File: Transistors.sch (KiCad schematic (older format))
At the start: 5 parts, among them T1 L298, T2 L298, T3 L298, T4 L298, T5 L298

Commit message: New schematics: Top and Controller
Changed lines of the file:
@@
 EESchema Schematic File Version 2
-LIBS:L298
 LIBS:power
 LIBS:device
@@
 LIBS:contrib
 LIBS:valves
-LIBS:Stepper Motor Driver-cache
+LIBS:L298
 EELAYER 25 0
 EELAYER END
 $Descr A4 11693 8268
 encoding utf-8
-Sheet 1 2
+Sheet 1 1
 Title ""
 Date ""
@@
 	1    0    0    -1
 $EndComp
-Text GLabel 1600 1500 0    60   Input ~ 0
+Text HLabel 1600 1600 0    60   Input ~ 0
+T1_Enable_A
+Text HLabel 1600 1700 0    60   Input ~ 0
+T1_Input_2
+Text HLabel 1600 1900 0    60   Input ~ 0
+T1_Input_3
+Text HLabel 1600 2000 0    60   Input ~ 0
+T1_Enable_B
+Text HLabel 1600 2100 0    60   Input ~ 0
+T1_Input_4
+Text HLabel 3650 1500 2    60   Input ~ 0
+T1_Output_1
+Text HLabel 3650 1600 2    60   Input ~ 0
+T1_Output_2
+Text HLabel 3650 1900 2    60   Input ~ 0
+T1_Output_3
+Text HLabel 3650 2000 2    60   Input ~ 0
+T1_Output_4
+Wire Wire Line
+	1600 1500 1900 1500
+Wire Wire Line
+	1600 1600 1900 1600
+Wire Wire Line
+	1600 1700 1900 1700
+Wire Wire Line
+	1600 1900 1900 1900
+Wire Wire Line
+	1600 2000 1900 2000
+Wire Wire Line
+	1600 2100 1900 2100
+Wire Wire Line
+	3400 1500 3650 1500
+Wire Wire Line
+	3400 1600 3650 1600
+Wire Wire Line
+	3400 1900 3650 1900
+Wire Wire Line
+	3400 2000 3650 2000
+Text HLabel 1600 3600 0    60   Input ~ 0
+T2_Input_1
+Text HLabel 1600 3700 0    60   Input ~ 0
+T2_Enable_A
+Text HLabel 1600 3800 0    60   Input ~ 0
+T2_Input_2
+Text HLabel 1600 4000 0    60   Input ~ 0
+T2_Input_3
+Text HLabel 1600 4100 0    60   Input ~ 0
+T2_Enable_B
+Text HLabel 1600 4200 0    60   Input ~ 0
+T2_Input_4
+Wire Wire Line
+	1600 3600 1900 3600
+Wire Wire Line
+	1600 3700 1900 3700
+Wire Wire Line
+	1600 3800 1900 3800
+Wire Wire Line
+	1600 4000 1900 4000
+Wire Wire Line
+	1600 4100 1900 4100
+Wire Wire Line
+	1600 4200 1900 4200
+Text HLabel 1600 5700 0    60   Input ~ 0
+T3_Input_1
+Text HLabel 1600 5800 0    60   Input ~ 0
+T3_Enable_A
+Text HLabel 1600 5900 0    60   Input ~ 0
+T3_Input_2
+Text HLabel 1600 6100 0    60   Input ~ 0
+T3_Input_3
+Text HLabel 1600 6200 0    60   Input ~ 0
+T3_Enable_B
+Text HLabel 1600 6300 0    60   Input ~ 0
+T3_Input_4
+Wire Wire Line
+	1600 5700 1900 5700
+Wire Wire Line
+	1600 5800 1900 5800
+Wire Wire Line
+	1600 5900 1900 5900
+Wire Wire Line
+	1600 6100 1900 6100
+Wire Wire Line
+	1600 6200 1900 6200
+Wire Wire Line
+	1600 6300 1900 6300
+Text HLabel 3650 3600 2    60   Input ~ 0
+T2_Output_1
+Text HLabel 3650 3700 2    60   Input ~ 0
+T2_Output_2
+Text HLabel 3650 4000 2    60   Input ~ 0
+T2_Output_3
+Text HLabel 3650 4100 2    60   Input ~ 0
+T2_Output_4
+Wire Wire Line
+	3400 3600 3650 3600
+Wire Wire Line
+	3400 3700 3650 3700
+Wire Wire Line
+	3400 4000 3650 4000
+Wire Wire Line
+	3400 4100 3650 4100
+Text HLabel 3650 5700 2    60   Input ~ 0
+T3_Output_1
+Text HLabel 3650 5800 2    60   Input ~ 0
+T3_Output_2
+Text HLabel 3650 6100 2    60   Input ~ 0
+T3_Output_3
+Text HLabel 3650 6200 2    60   Input ~ 0
+T3_Output_4
+Wire Wire Line
+	3400 5700 3650 5700
+Wire Wire Line
+	3400 5800 3650 5800
+Wire Wire Line
+	3400 6100 3650 6100
+Wire Wire Line
+	3400 6200 3650 6200
+Text HLabel 8100 1600 2    60   Input ~ 0
+T4_Output_1
+Text HLabel 8100 1700 2    60   Input ~ 0
+T4_Output_2
+Text HLabel 8100 2000 2    60   Input ~ 0
+T4_Output_3
+Text HLabel 8100 2100 2    60   Input ~ 0
+T4_Output_4
+Wire Wire Line
+	7850 1600 8100 1600
+Wire Wire Line
+	7850 1700 8100 1700
+Wire Wire Line
+	7850 2000 8100 2000
+Wire Wire Line
+	7850 2100 8100 2100
+Text HLabel 8100 3650 2    60   Input ~ 0
+T5_Output_1
+Text HLabel 8100 3750 2    60   Input ~ 0
+T5_Output_2
+Text HLabel 8100 4050 2    60   Input ~ 0
+T5_Output_3
+Text HLabel 8100 4150 2    60   Input ~ 0
+T5_Output_4
+Wire Wire Line
+	7850 3650 8100 3650
+Wire Wire Line
+	7850 3750 8100 3750
+Wire Wire Line
+	7850 4050 8100 4050
+Wire Wire Line
+	7850 4150 8100 4150
+Text HLabel 6050 1600 0    60   Input ~ 0
+T4_Input_1
+Text HLabel 6050 1700 0    60   Input ~ 0
+T4_Enable_A
+Text HLabel 6050 1800 0    60   Input ~ 0
+T4_Input_2
+Text HLabel 6050 2000 0    60   Input ~ 0
+T4_Input_3
+Text HLabel 6050 2100 0    60   Input ~ 0
+T4_Enable_B
+Text HLabel 6050 2200 0    60   Input ~ 0
+T4_Input_4
+Wire Wire Line
+	6050 1600 6350 1600
+Wire Wire Line
+	6050 1700 6350 1700
+Wire Wire Line
+	6050 1800 6350 1800
+Wire Wire Line
+	6050 2000 6350 2000
+Wire Wire Line
+	6050 2100 6350 2100
+Wire Wire Line
+	6050 2200 6350 2200
+Text HLabel 6050 3650 0    60   Input ~ 0
+T5_Input_1
+Text HLabel 6050 3750 0    60   Input ~ 0
+T5_Enable_A
+Text HLabel 6050 3850 0    60   Input ~ 0
+T5_Input_2
+Text HLabel 6050 4050 0    60   Input ~ 0
+T5_Input_3
+Text HLabel 6050 4150 0    60   Input ~ 0
+T5_Enable_B
+Text HLabel 6050 4250 0    60   Input ~ 0
+T5_Input_4
+Wire Wire Line
+	6050 3650 6350 3650
+Wire Wire Line
+	6050 3750 6350 3750
+Wire Wire Line
+	6050 3850 6350 3850
+Wire Wire Line
+	6050 4050 6350 4050
+Wire Wire Line
+	6050 4150 6350 4150
+Wire Wire Line
+	6050 4250 6350 4250
+Text HLabel 1600 1500 0    60   Input ~ 0
 T1_Input_1
-Text GLabel 1600 1600 0    60   Input ~ 0
-T1_Enable_A
-Text GLabel 1600 1700 0    60   Input ~ 0
-T1_Input_2
-Text GLabel 1600 1900 0    60   Input ~ 0
-T1_Input_3
-Text GLabel 1600 2000 0    60   Input ~ 0
-T1_Enable_B
-Text GLabel 1600 2100 0    60   Input ~ 0
-T1_Input_4
-Text GLabel 3650 1500 2    60   Input ~ 0
-T1_Output_1
-Text GLabel 3650 1600 2    60   Input ~ 0
-T1_Output_2
-Text GLabel 3650 1900 2    60   Input ~ 0
-T1_Output_3
-Text GLabel 3650 2000 2    60   Input ~ 0
-T1_Output_4
-Wire Wire Line
-	1600 1500 1900 1500
-Wire Wire Line
-	1600 1600 1900 1600
-Wire Wire Line
-	1600 1700 1900 1700
-Wire Wire Line
-	1600 1900 1900 1900
-Wire Wire Line
-	1600 2000 1900 2000
-Wire Wire Line
-	1600 2100 1900 2100
-Wire Wire Line
-	3400 1500 3650 1500
-Wire Wire Line
-	3400 1600 3650 1600
-Wire Wire Line
-	3400 1900 3650 1900
-Wire Wire Line
-	3400 2000 3650 2000
-Text GLabel 1600 3600 0    60   Input ~ 0
-T2_Input_1
-Text GLabel 1600 3700 0    60   Input ~ 0
-T2_Enable_A
-Text GLabel 1600 3800 0    60   Input ~ 0
-T2_Input_2
-Text GLabel 1600 4000 0    60   Input ~ 0
-T2_Input_3
-Text GLabel 1600 4100 0    60   Input ~ 0
-T2_Enable_B
-Text GLabel 1600 4200 0    60   Input ~ 0
-T2_Input_4
-Wire Wire Line
-	1600 3600 1900 3600
-Wire Wire Line
-	1600 3700 1900 3700
-Wire Wire Line
-	1600 3800 1900 3800
-Wire Wire Line
-	1600 4000 1900 4000
-Wire Wire Line
-	1600 4100 1900 4100
-Wire Wire Line
-	1600 4200 1900 4200
-Text GLabel 1600 5700 0    60   Input ~ 0
-T3_Input_1
-Text GLabel 1600 5800 0    60   Input ~ 0
-T3_Enable_A
-Text GLabel 1600 5900 0    60   Input ~ 0
-T3_Input_2
-Text GLabel 1600 6100 0    60   Input ~ 0
-T3_Input_3
-Text GLabel 1600 6200 0    60   Input ~ 0
-T3_Enable_B
-Text GLabel 1600 6300 0    60   Input ~ 0
-T3_Input_4
-Wire Wire Line
-	1600 5700 1900 5700
-Wire Wire Line
-	1600 5800 1900 5800
-Wire Wire Line
-	1600 5900 1900 5900
-Wire Wire Line
-	1600 6100 1900 6100
-Wire Wire Line
-	1600 6200 1900 6200
-Wire Wire Line
-	1600 6300 1900 6300
-Text GLabel 3650 3600 2    60   Input ~ 0
-T2_Output_1
-Text GLabel 3650 3700 2    60   Input ~ 0
-T2_Output_2
-Text GLabel 3650 4000 2    60   Input ~ 0
-T2_Output_3
-Text GLabel 3650 4100 2    60   Input ~ 0
-T2_Output_4
-Wire Wire Line
-	3400 3600 3650 3600
-Wire Wire Line
-	3400 3700 3650 3700
-Wire Wire Line
-	3400 4000 3650 4000
-Wire Wire Line
-	3400 4100 3650 4100
-Text GLabel 3650 5700 2    60   Input ~ 0
-T3_Output_1
-Text GLabel 3650 5800 2    60   Input ~ 0
-T3_Output_2
-Text GLabel 3650 6100 2    60   Input ~ 0
-T3_Output_3
-Text GLabel 3650 6200 2    60   Input ~ 0
-T3_Output_4
-Wire Wire Line
-	3400 5700 3650 5700
-Wire Wire Line
-	3400 5800 3650 5800
-Wire Wire Line
-	3400 6100 3650 6100
-Wire Wire Line
-	3400 6200 3650 6200
-Text GLabel 8100 1600 2    60   Input ~ 0
-T4_Output_1
-Text GLabel 8100 1700 2    60   Input ~ 0
-T4_Output_2
-Text GLabel 8100 2000 2    60   Input ~ 0
-T4_Output_3
-Text GLabel 8100 2100 2    60   Input ~ 0
-T4_Output_4
-Wire Wire Line
-	7850 1600 8100 1600
-Wire Wire Line
-	7850 1700 8100 1700
-Wire Wire Line
-	7850 2000 8100 2000
-Wire Wire Line
-	7850 2100 8100 2100
-Text GLabel 8100 3650 2    60   Input ~ 0
-T5_Output_1
-Text GLabel 8100 3750 2    60   Input ~ 0
-T5_Output_2
-Text GLabel 8100 4050 2    60   Input ~ 0
-T5_Output_3
-Text GLabel 8100 4150 2    60   Input ~ 0
-T5_Output_4
-Wire Wire Line
-	7850 3650 8100 3650
-Wire Wire Line
-	7850 3750 8100 3750
-Wire Wire Line
-	7850 4050 8100 4050
-Wire Wire Line
-	7850 4150 8100 4150
-Text GLabel 6050 1600 0    60   Input ~ 0
-T4_Input_1
-Text GLabel 6050 1700 0    60   Input ~ 0
-T4_Enable_A
-Text GLabel 6050 1800 0    60   Input ~ 0
-T4_Input_2
-Text GLabel 6050 2000 0    60   Input ~ 0
-T4_Input_3
-Text GLabel 6050 2100 0    60   Input ~ 0
-T4_Enable_B
-Text GLabel 6050 2200 0    60   Input ~ 0
-T4_Input_4
-Wire Wire Line
-	6050 1600 6350 1600
-Wire Wire Line
-	6050 1700 6350 1700
-Wire Wire Line
-	6050 1800 6350 1800
-Wire Wire Line
-	6050 2000 6350 2000
-Wire Wire Line
-	6050 2100 6350 2100
-Wire Wire Line
-	6050 2200 6350 2200
-Text GLabel 6050 3650 0    60   Input ~ 0
-T5_Input_1
-Text GLabel 6050 3750 0    60   Input ~ 0
-T5_Enable_A
-Text GLabel 6050 3850 0    60   Input ~ 0
-T5_Input_2
-Text GLabel 6050 4050 0    60   Input ~ 0
-T5_Input_3
-Text GLabel 6050 4150 0    60   Input ~ 0
-T5_Enable_B
-Text GLabel 6050 4250 0    60   Input ~ 0
-T5_Input_4
-Wire Wire Line
-	6050 3650 6350 3650
-Wire Wire Line
-	6050 3750 6350 3750
-Wire Wire Line
-	6050 3850 6350 3850
-Wire Wire Line
-	6050 4050 6350 4050
-Wire Wire Line
-	6050 4150 6350 4150
-Wire Wire Line
-	6050 4250 6350 4250
 $EndSCHEMATC

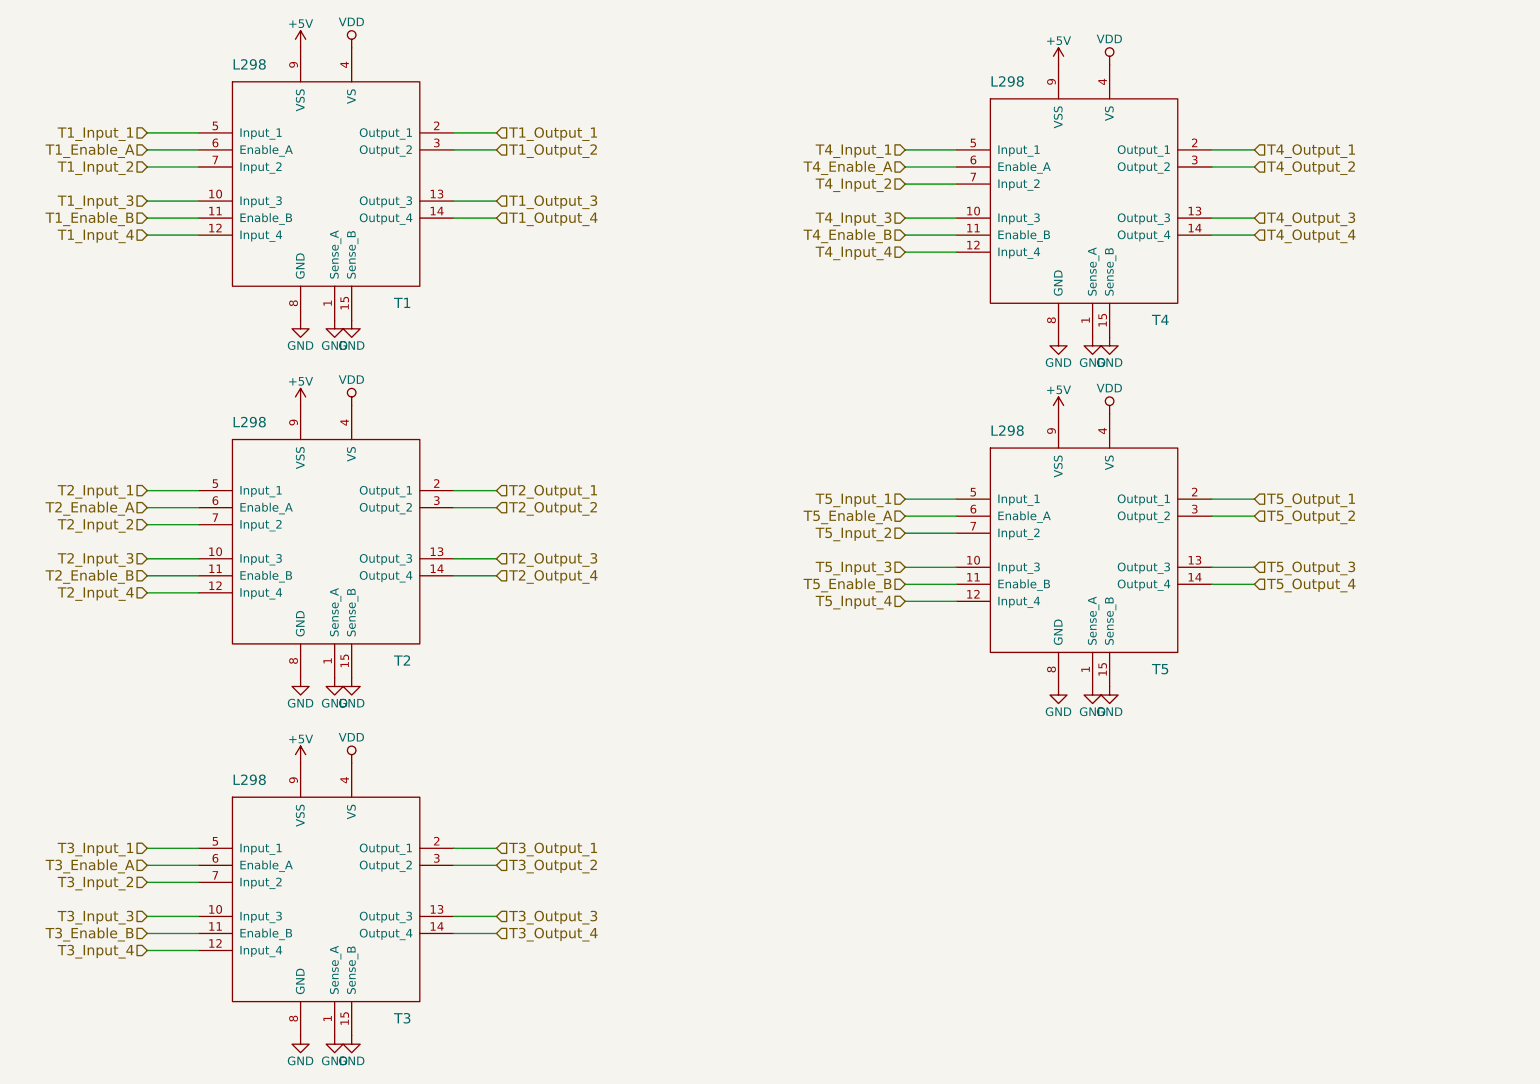
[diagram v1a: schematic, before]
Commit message: Designed Transistors.sch as hierarchical schematic importing 5x L298.sch
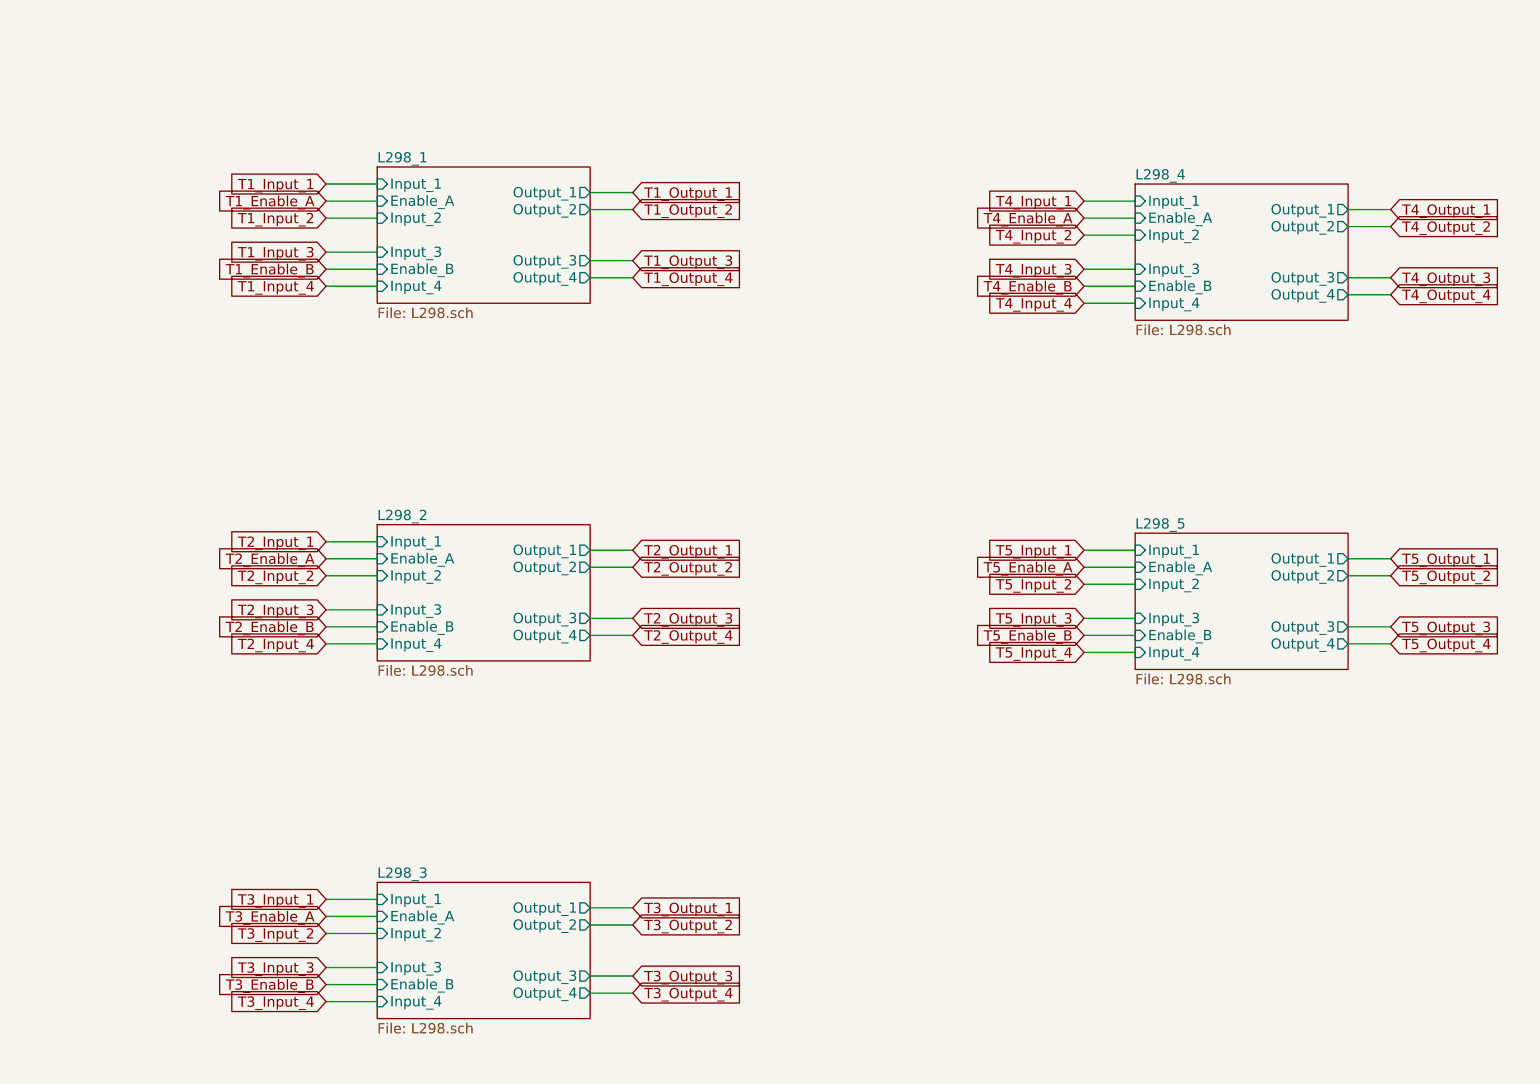
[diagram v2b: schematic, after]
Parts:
- removed T1, T2, T3, T4, T5: L298, Multiwatt15, symbol L298
